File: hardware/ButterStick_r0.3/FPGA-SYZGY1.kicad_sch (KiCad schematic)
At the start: 1 part, among them U2 ECP5UM5G_85_CABGA381

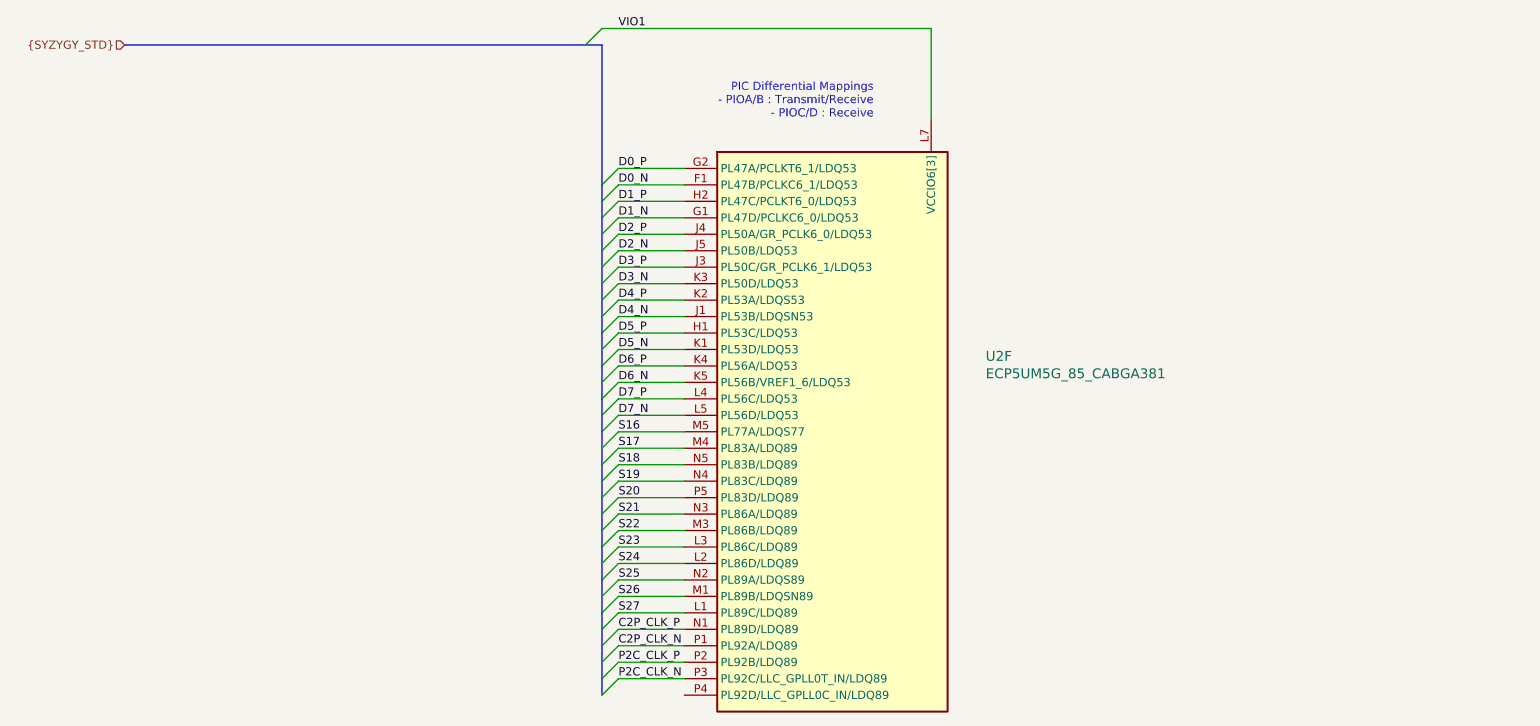
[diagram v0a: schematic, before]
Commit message: hw.r0_3: routing improvements
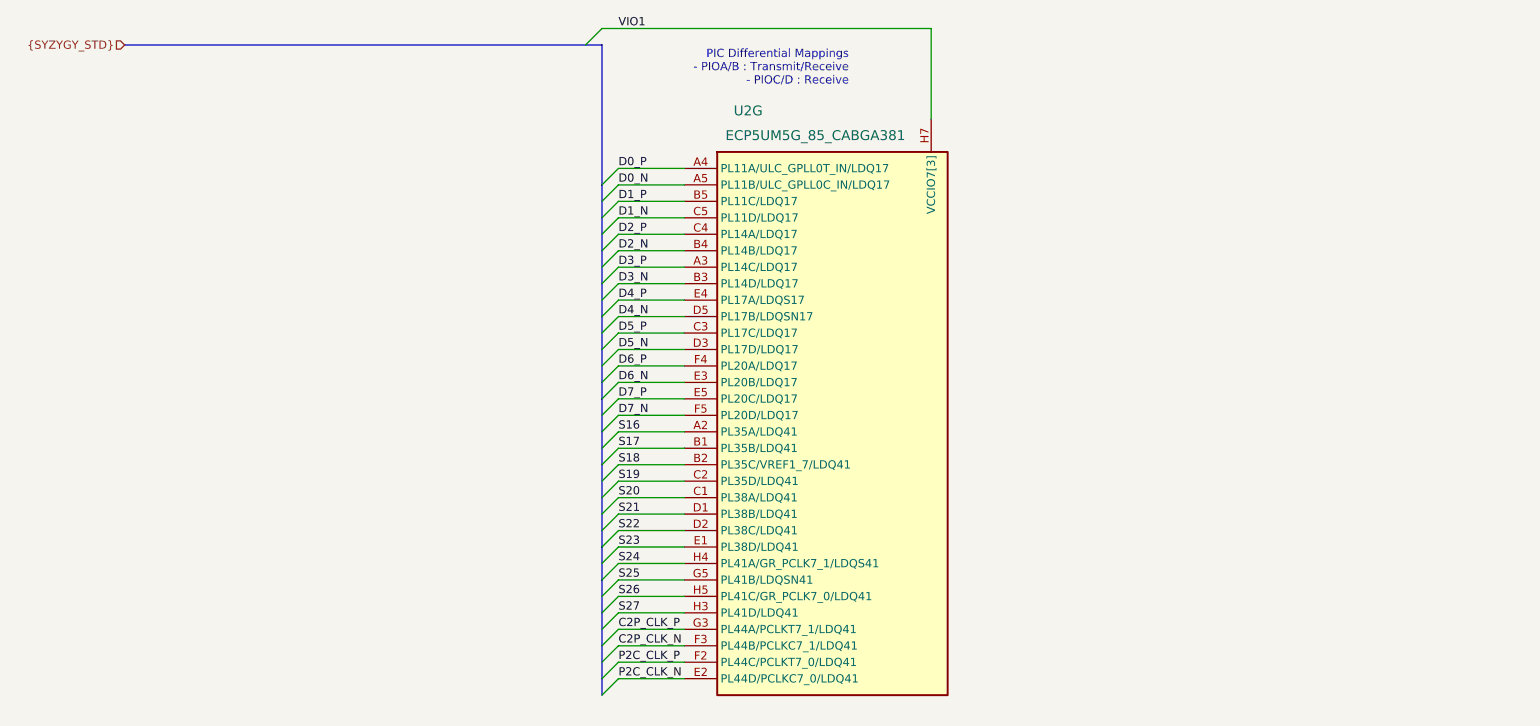
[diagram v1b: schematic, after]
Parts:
- removed U2: ECP5UM5G_85_CABGA381, gkl_housings_bga:caBGA_381_17x17, symbol gkl_lattice:ECP5UM5G_85_CABGA381
- added U2: ECP5UM5G_85_CABGA381, gkl_housings_bga:caBGA_381_17x17, symbol gkl_lattice:ECP5UM5G_85_CABGA381
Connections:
- net C2P_CLK_N: now also U2.F3 (PL44B/PCLKC7_1/LDQ41)
- net C2P_CLK_P: now also U2.G3 (PL44A/PCLKT7_1/LDQ41)
- net D0_N: now also U2.A5 (PL11B/ULC_GPLL0C_IN/LDQ17)
- net D0_P: now also U2.A4 (PL11A/ULC_GPLL0T_IN/LDQ17)
- net D1_N: now also U2.C5 (PL11D/LDQ17)
- net D1_P: now also U2.B5 (PL11C/LDQ17)
- net D2_N: now also U2.B4 (PL14B/LDQ17)
- net D2_P: now also U2.C4 (PL14A/LDQ17)
- net D3_N: now also U2.B3 (PL14D/LDQ17)
- net D3_P: now also U2.A3 (PL14C/LDQ17)
- net D4_N: now also U2.D5 (PL17B/LDQSN17)
- net D4_P: now also U2.E4 (PL17A/LDQS17)
- net D5_N: now also U2.D3 (PL17D/LDQ17)
- net D5_P: now also U2.C3 (PL17C/LDQ17)
- net D6_N: now also U2.E3 (PL20B/LDQ17)
- net D6_P: now also U2.F4 (PL20A/LDQ17)
- net D7_N: now also U2.F5 (PL20D/LDQ17)
- net D7_P: now also U2.E5 (PL20C/LDQ17)
- net P2C_CLK_N: now also U2.E2 (PL44D/PCLKC7_0/LDQ41)
- net P2C_CLK_P: now also U2.F2 (PL44C/PCLKT7_0/LDQ41)
- net S16: now also U2.A2 (PL35A/LDQ41)
- net S17: now also U2.B1 (PL35B/LDQ41)
- net S18: now also U2.B2 (PL35C/VREF1_7/LDQ41)
- net S19: now also U2.C2 (PL35D/LDQ41)
- net S20: now also U2.C1 (PL38A/LDQ41)
- net S21: now also U2.D1 (PL38B/LDQ41)
- net S22: now also U2.D2 (PL38C/LDQ41)
- net S23: now also U2.E1 (PL38D/LDQ41)
- net S24: now also U2.H4 (PL41A/GR_PCLK7_1/LDQS41)
- net S25: now also U2.G5 (PL41B/LDQSN41)
- net S26: now also U2.H5 (PL41C/GR_PCLK7_0/LDQ41)
- net S27: now also U2.H3 (PL41D/LDQ41)
- net VIO1: now also U2.H6 (VCCIO7[3]), U2.H7 (VCCIO7[3]), U2.J6 (VCCIO7[3])
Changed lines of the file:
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@@
 (kicad_sch (version 20200512) (host eeschema "5.99.0-unknown-c8476d6~101~ubuntu18.04.1")
-  (page 11 20)
+  (page 1 20)
   (paper "A4")
   (bus_entry (at 104.14 52.07) (size 2.54 -2.54))
@@
   (bus (pts (xy 106.68 83.82) (xy 106.68 88.9)))
   (bus (pts (xy 106.68 88.9) (xy 106.68 93.98)))
-  (bus (pts (xy 106.68 93.98) (xy 106.68 96.52)))
-  (bus (pts (xy 106.68 96.52) (xy 106.68 101.6)))
-  (bus (pts (xy 106.68 101.6) (xy 106.68 106.68)))
+  (bus (pts (xy 106.68 93.98) (xy 106.68 99.06)))
+  (bus (pts (xy 106.68 99.06) (xy 106.68 104.14)))
+  (bus (pts (xy 106.68 104.14) (xy 106.68 106.68)))
   (bus (pts (xy 106.68 106.68) (xy 106.68 111.76)))
   (bus (pts (xy 106.68 111.76) (xy 106.68 116.84)))
@@
   (bus (pts (xy 106.68 149.86) (xy 106.68 152.4)))
   (text "PIC Differential Mappings\n - PIOA/B : Transmit/Receive\n - PIOC/D : Receive"
-    (at 148.59 63.5 0)
+    (at 144.78 58.42 0)
     (effects (font (size 1.27 1.27)) (justify right bottom))
   )
@@
     (effects (font (size 1.27 1.27)) (justify right))
   )
-  (symbol (lib_id "gkl_lattice:ECP5UM5G_85_CABGA381") (at 119.38 71.12 0) (unit 6)
-    (property "Reference" "U2" (id 0) (at 165.8874 100.1014 0)
+  (symbol (lib_id "gkl_lattice:ECP5UM5G_85_CABGA381") (at 119.38 71.12 0) (unit 7)
+    (property "Reference" "U2" (id 0) (at 127 62.23 0)
       (effects (font (size 1.524 1.524)) (justify left))
     )
-    (property "Value" "ECP5UM5G_85_CABGA381" (id 1) (at 165.8874 102.7938 0)
+    (property "Value" "ECP5UM5G_85_CABGA381" (id 1) (at 125.73 66.04 0)
       (effects (font (size 1.524 1.524)) (justify left))
     )

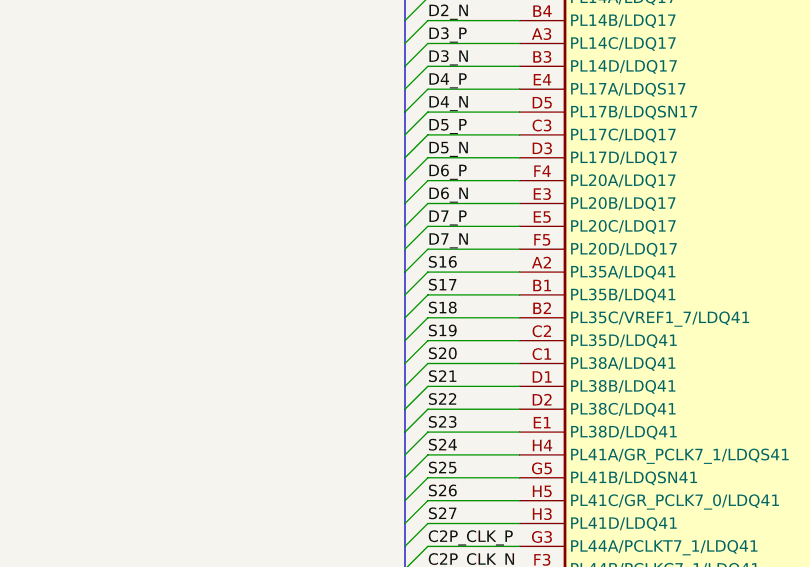
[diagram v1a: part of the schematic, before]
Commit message: hw.r0_3: Start routing DDR3 interface
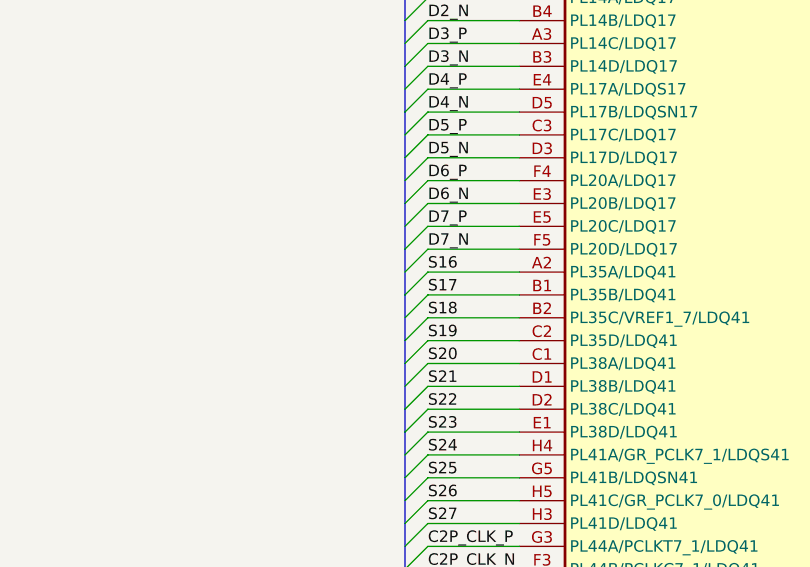
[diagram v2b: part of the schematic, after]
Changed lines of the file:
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@@
-(kicad_sch (version 20200512) (host eeschema "5.99.0-unknown-c8476d6~101~ubuntu18.04.1")
+(kicad_sch (version 20200512) (host eeschema "5.99.0-unknown-711fc99~101~ubuntu18.04.1")
   (page 1 20)
   (paper "A4")
@@
   (bus (pts (xy 106.68 93.98) (xy 106.68 99.06)))
   (bus (pts (xy 106.68 99.06) (xy 106.68 104.14)))
-  (bus (pts (xy 106.68 104.14) (xy 106.68 106.68)))
-  (bus (pts (xy 106.68 106.68) (xy 106.68 111.76)))
-  (bus (pts (xy 106.68 111.76) (xy 106.68 116.84)))
-  (bus (pts (xy 106.68 116.84) (xy 106.68 121.92)))
+  (bus (pts (xy 106.68 104.14) (xy 106.68 109.22)))
+  (bus (pts (xy 106.68 109.22) (xy 106.68 114.3)))
+  (bus (pts (xy 106.68 114.3) (xy 106.68 119.38)))
+  (bus (pts (xy 106.68 119.38) (xy 106.68 121.92)))
   (bus (pts (xy 106.68 121.92) (xy 106.68 127)))
   (bus (pts (xy 106.68 127) (xy 106.68 129.54)))

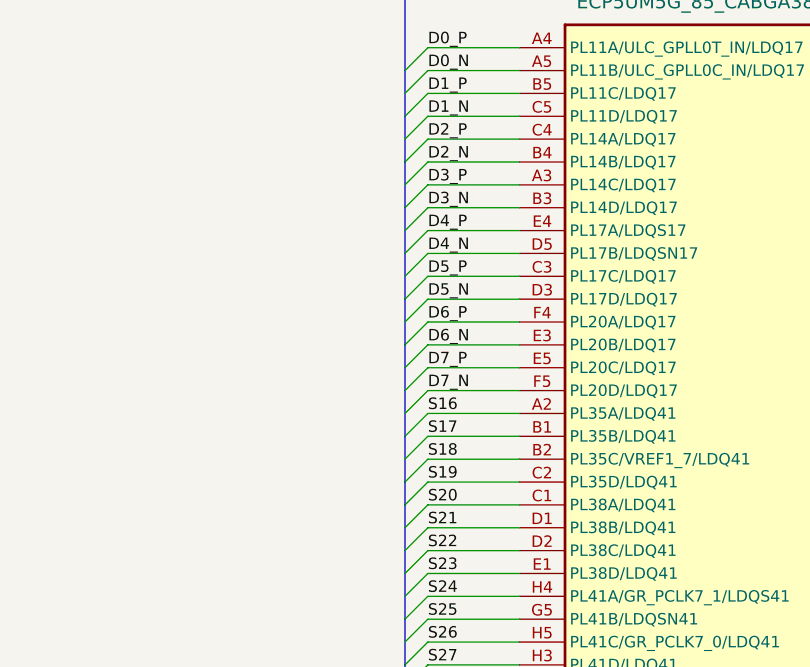
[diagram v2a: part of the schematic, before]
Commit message: hw.r0_3: Inital routing of DDR3 done
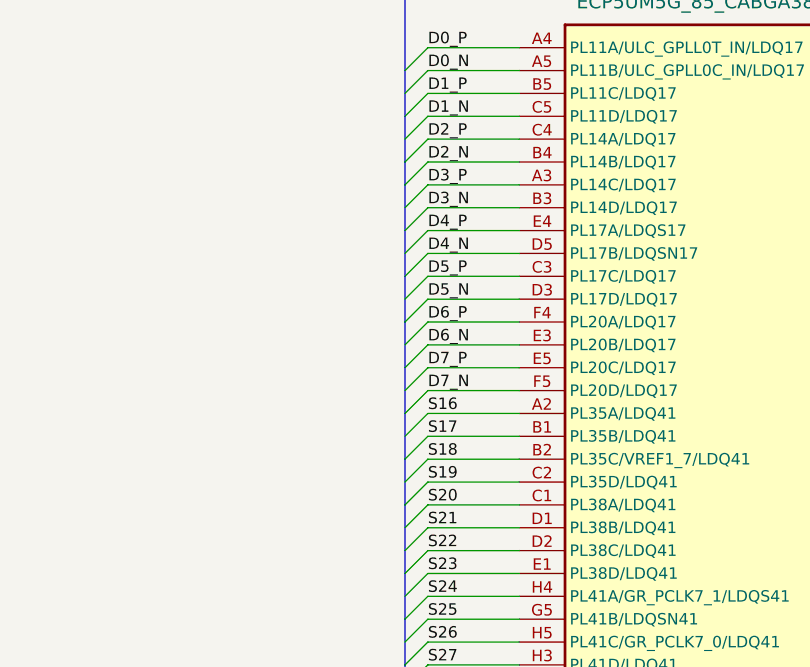
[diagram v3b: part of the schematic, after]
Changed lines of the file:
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@@
   (bus (pts (xy 106.68 73.66) (xy 106.68 78.74)))
   (bus (pts (xy 106.68 78.74) (xy 106.68 83.82)))
-  (bus (pts (xy 106.68 83.82) (xy 106.68 88.9)))
-  (bus (pts (xy 106.68 88.9) (xy 106.68 93.98)))
-  (bus (pts (xy 106.68 93.98) (xy 106.68 99.06)))
-  (bus (pts (xy 106.68 99.06) (xy 106.68 104.14)))
-  (bus (pts (xy 106.68 104.14) (xy 106.68 109.22)))
-  (bus (pts (xy 106.68 109.22) (xy 106.68 114.3)))
-  (bus (pts (xy 106.68 114.3) (xy 106.68 119.38)))
-  (bus (pts (xy 106.68 119.38) (xy 106.68 121.92)))
+  (bus (pts (xy 106.68 83.82) (xy 106.68 86.36)))
+  (bus (pts (xy 106.68 86.36) (xy 106.68 91.44)))
+  (bus (pts (xy 106.68 91.44) (xy 106.68 96.52)))
+  (bus (pts (xy 106.68 96.52) (xy 106.68 101.6)))
+  (bus (pts (xy 106.68 101.6) (xy 106.68 106.68)))
+  (bus (pts (xy 106.68 106.68) (xy 106.68 111.76)))
+  (bus (pts (xy 106.68 111.76) (xy 106.68 116.84)))
+  (bus (pts (xy 106.68 116.84) (xy 106.68 121.92)))
   (bus (pts (xy 106.68 121.92) (xy 106.68 127)))
   (bus (pts (xy 106.68 127) (xy 106.68 129.54)))

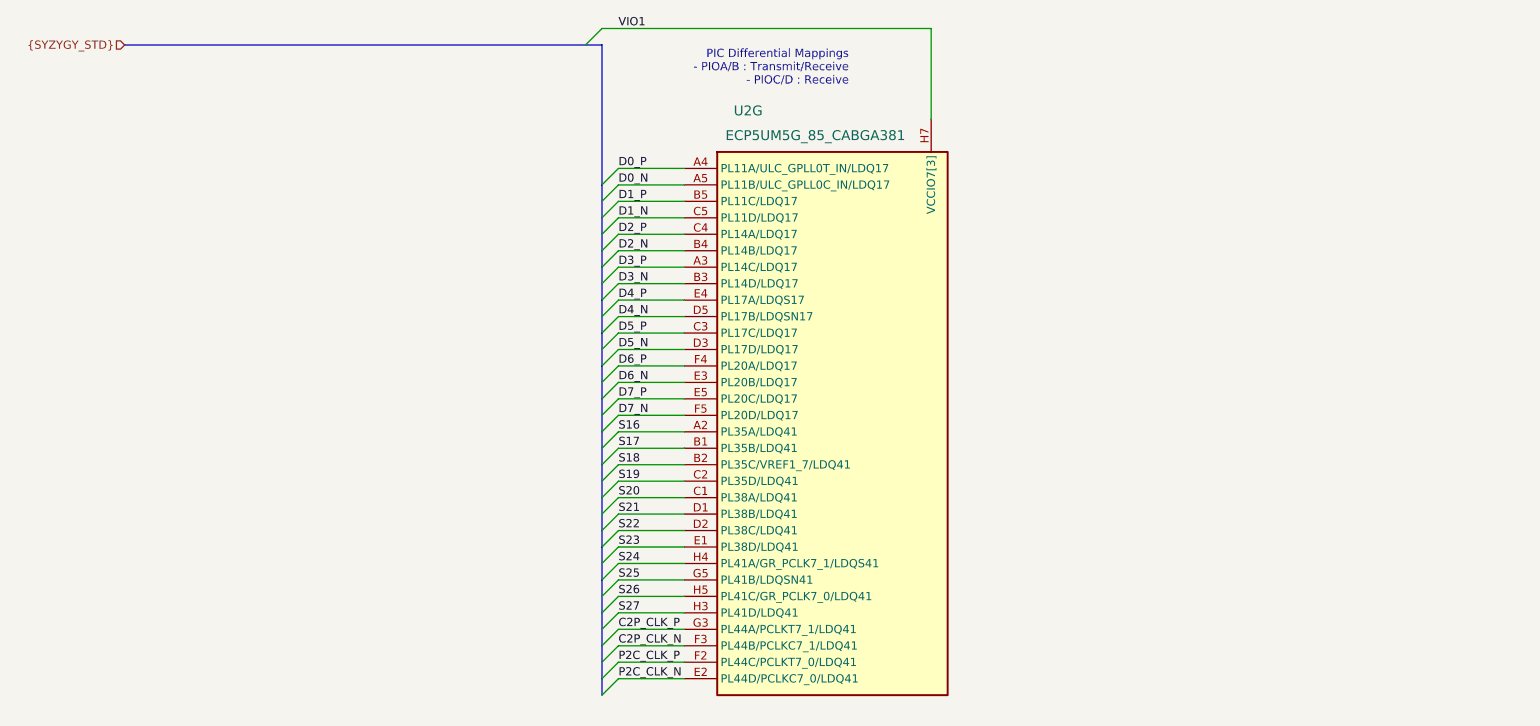
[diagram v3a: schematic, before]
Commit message: hw.r0_3: routed SYZYGY, begin routing RGMII/ULPI
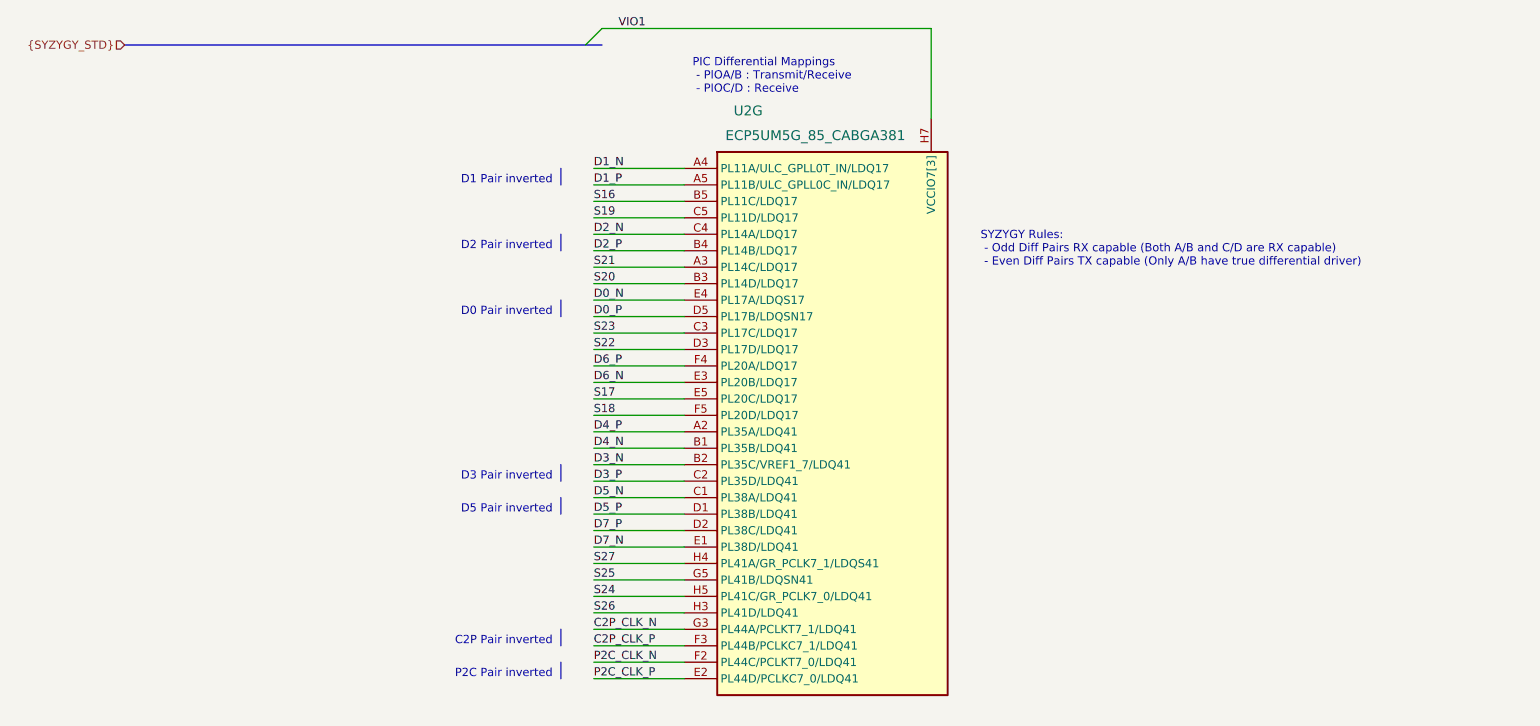
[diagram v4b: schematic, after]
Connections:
- net C2P_CLK_N: now also U2.G3 (PL44A/PCLKT7_1/LDQ41); no longer U2.F3 (PL44B/PCLKC7_1/LDQ41)
- net C2P_CLK_P: now also U2.F3 (PL44B/PCLKC7_1/LDQ41); no longer U2.G3 (PL44A/PCLKT7_1/LDQ41)
- net D0_N: now also U2.E4 (PL17A/LDQS17); no longer U2.A5 (PL11B/ULC_GPLL0C_IN/LDQ17)
- net D0_P: now also U2.D5 (PL17B/LDQSN17); no longer U2.A4 (PL11A/ULC_GPLL0T_IN/LDQ17)
- net D1_N: now also U2.A4 (PL11A/ULC_GPLL0T_IN/LDQ17); no longer U2.C5 (PL11D/LDQ17)
- net D1_P: now also U2.A5 (PL11B/ULC_GPLL0C_IN/LDQ17); no longer U2.B5 (PL11C/LDQ17)
- net D2_N: now also U2.C4 (PL14A/LDQ17); no longer U2.B4 (PL14B/LDQ17)
- net D2_P: now also U2.B4 (PL14B/LDQ17); no longer U2.C4 (PL14A/LDQ17)
- net D3_N: now also U2.B2 (PL35C/VREF1_7/LDQ41); no longer U2.B3 (PL14D/LDQ17)
- net D3_P: now also U2.C2 (PL35D/LDQ41); no longer U2.A3 (PL14C/LDQ17)
- net D4_N: now also U2.B1 (PL35B/LDQ41); no longer U2.D5 (PL17B/LDQSN17)
- net D4_P: now also U2.A2 (PL35A/LDQ41); no longer U2.E4 (PL17A/LDQS17)
- net D5_N: now also U2.C1 (PL38A/LDQ41); no longer U2.D3 (PL17D/LDQ17)
- net D5_P: now also U2.D1 (PL38B/LDQ41); no longer U2.C3 (PL17C/LDQ17)
- net D7_N: now also U2.E1 (PL38D/LDQ41); no longer U2.F5 (PL20D/LDQ17)
- net D7_P: now also U2.D2 (PL38C/LDQ41); no longer U2.E5 (PL20C/LDQ17)
- net P2C_CLK_N: now also U2.F2 (PL44C/PCLKT7_0/LDQ41); no longer U2.E2 (PL44D/PCLKC7_0/LDQ41)
- net P2C_CLK_P: now also U2.E2 (PL44D/PCLKC7_0/LDQ41); no longer U2.F2 (PL44C/PCLKT7_0/LDQ41)
- net S16: now also U2.B5 (PL11C/LDQ17); no longer U2.A2 (PL35A/LDQ41)
- net S17: now also U2.E5 (PL20C/LDQ17); no longer U2.B1 (PL35B/LDQ41)
- net S18: now also U2.F5 (PL20D/LDQ17); no longer U2.B2 (PL35C/VREF1_7/LDQ41)
- net S19: now also U2.C5 (PL11D/LDQ17); no longer U2.C2 (PL35D/LDQ41)
- net S20: now also U2.B3 (PL14D/LDQ17); no longer U2.C1 (PL38A/LDQ41)
- net S21: now also U2.A3 (PL14C/LDQ17); no longer U2.D1 (PL38B/LDQ41)
- net S22: now also U2.D3 (PL17D/LDQ17); no longer U2.D2 (PL38C/LDQ41)
- net S23: now also U2.C3 (PL17C/LDQ17); no longer U2.E1 (PL38D/LDQ41)
- net S24: now also U2.H5 (PL41C/GR_PCLK7_0/LDQ41); no longer U2.H4 (PL41A/GR_PCLK7_1/LDQS41)
- net S26: now also U2.H3 (PL41D/LDQ41); no longer U2.H5 (PL41C/GR_PCLK7_0/LDQ41)
- net S27: now also U2.H4 (PL41A/GR_PCLK7_1/LDQS41); no longer U2.H3 (PL41D/LDQ41)
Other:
- note added: "C2P Pair inverted"
- note added: "D0 Pair inverted"
- note added: "D1 Pair inverted"
- note added: "D2 Pair inverted"
- note added: "D3 Pair inverted"
- note added: "D5 Pair inverted"
- note added: "P2C Pair inverted"
- note added: "SYZYGY Rules: - Odd Diff Pairs RX capable (Both A/B and C/D are RX capable) - Even Diff Pairs TX capable (Only A/B have true differential driver)"

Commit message: hw.r0_3: major blocks roughly routed
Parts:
- renumbered U2 to U4
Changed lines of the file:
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@@
   )
   (symbol (lib_id "gkl_lattice:ECP5UM5G_85_CABGA381") (at 119.38 71.12 0) (unit 7)
-    (property "Reference" "U2" (id 0) (at 127 62.23 0)
+    (property "Reference" "U4" (id 0) (at 127 62.23 0)
       (effects (font (size 1.524 1.524)) (justify left))
     )
